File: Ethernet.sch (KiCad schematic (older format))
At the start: 26 parts, among them U5 DM9000B, U6 93LC46, U8 Pulse-J00-0045NL, Y1 25MHz

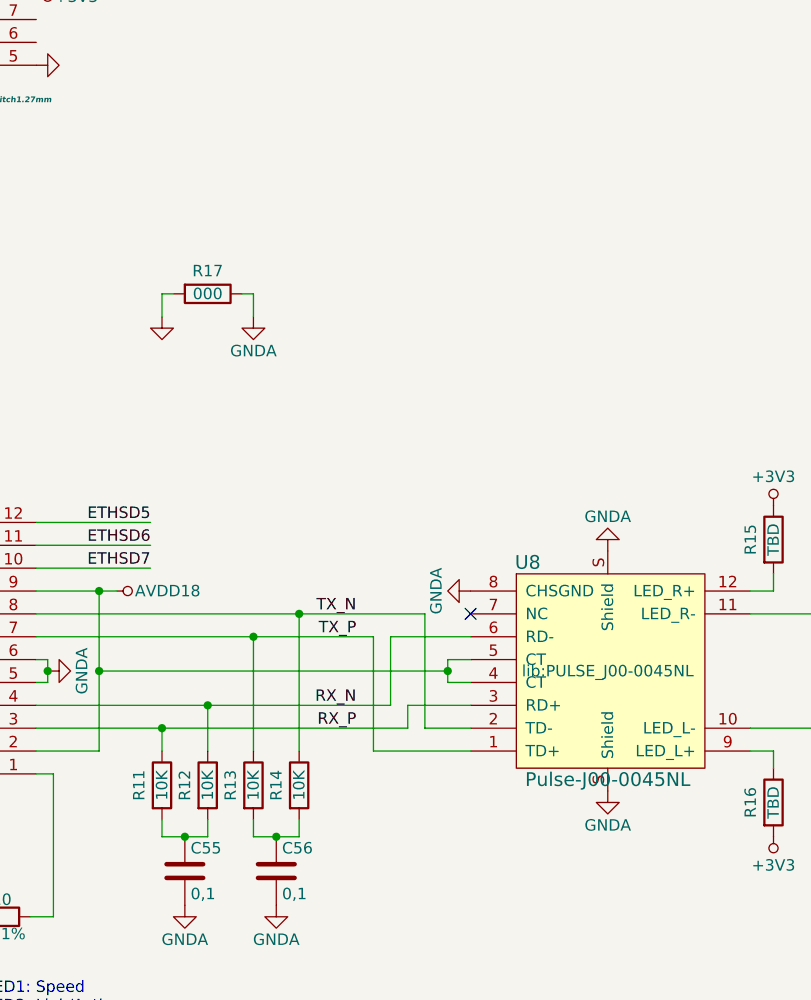
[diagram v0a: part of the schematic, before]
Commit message: Shield copper pour for RJ45
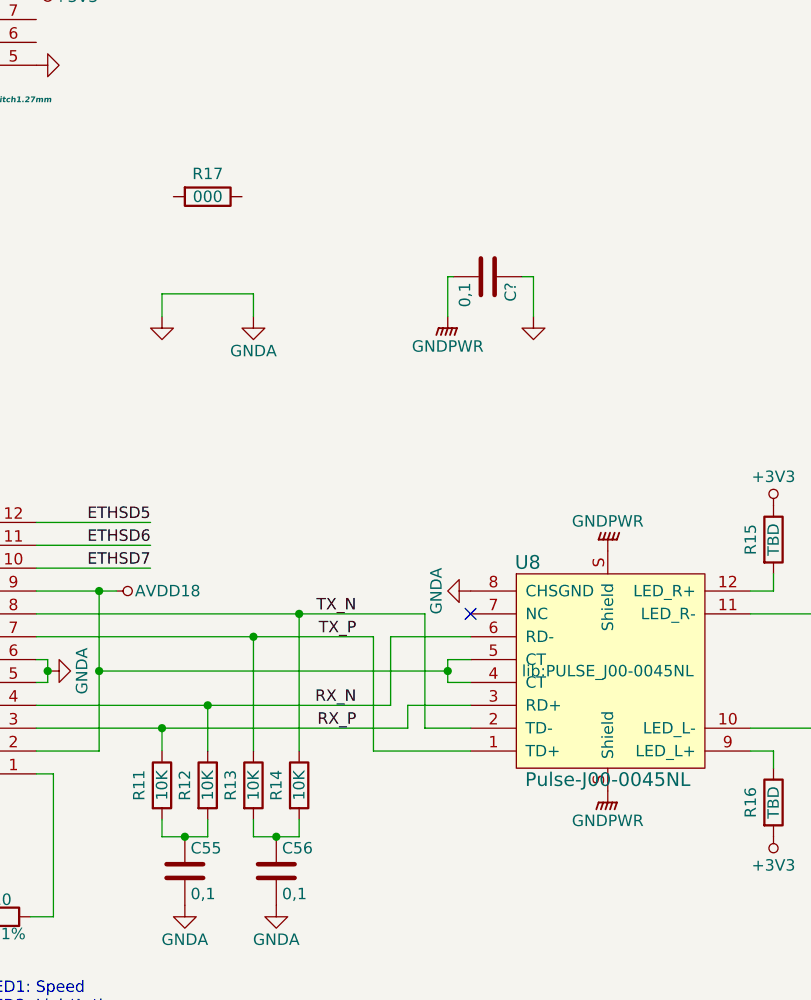
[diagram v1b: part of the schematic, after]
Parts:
- added C?: 0,1, Capacitors_SMD:C_0603, symbol C
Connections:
- net GND: now also C55.2, C56.2, R10.2, U5.47 (RXGND), U5.48 (BGGND), U5.5 (RXGND), U5.6 (TXGND), U8.8 (CHSGND), C?.1; no longer R17.2
- removed net GNDA: C55.2, C56.2, R10.2, R17.1, U5.47 (RXGND), U5.48 (BGGND), U5.5 (RXGND), U5.6 (TXGND), U8.8 (CHSGND), U8.S (Shield)
- new net GNDPWR: C?.2, U8.S (Shield)
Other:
- moved on the sheet: R17
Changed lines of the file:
@@
 $EndComp
 $Comp
-L GND #PWR110
+L GND #PWR0103
 U 1 1 58094372
 P 4850 5575
-F 0 "#PWR110" H 4850 5325 50  0001 C CNN
+F 0 "#PWR0103" H 4850 5325 50  0001 C CNN
 F 1 "GND" H 4850 5425 50  0001 C CNN
 F 2 "" H 4850 5575 50  0000 C CNN
@@
 Connection ~ 4950 6625
 $Comp
-L GNDA #PWR119
+L GNDA #PWR0104
 U 1 1 580972E8
 P 5550 5650
-F 0 "#PWR119" H 5550 5400 50  0001 C CNN
+F 0 "#PWR0104" H 5550 5400 50  0001 C CNN
 F 1 "GNDA" H 5550 5500 50  0000 C CNN
 F 2 "" H 5550 5650 50  0000 C CNN
@@
 Connection ~ 5550 5650
 $Comp
-L GND #PWR115
+L GND #PWR0105
 U 1 1 58097964
 P 5250 5575
-F 0 "#PWR115" H 5250 5325 50  0001 C CNN
+F 0 "#PWR0105" H 5250 5325 50  0001 C CNN
 F 1 "GND" H 5250 5425 50  0001 C CNN
 F 2 "" H 5250 5575 50  0000 C CNN
@@
 $EndComp
 $Comp
-L GND #PWR117
+L GND #PWR0106
 U 1 1 5809797E
 P 5350 3375
-F 0 "#PWR117" H 5350 3125 50  0001 C CNN
+F 0 "#PWR0106" H 5350 3125 50  0001 C CNN
 F 1 "GND" H 5350 3225 50  0001 C CNN
 F 2 "" H 5350 3375 50  0000 C CNN
@@
 $EndComp
 $Comp
-L GND #PWR108
+L GND #PWR0107
 U 1 1 580979A7
 P 3900 4725
-F 0 "#PWR108" H 3900 4475 50  0001 C CNN
+F 0 "#PWR0107" H 3900 4475 50  0001 C CNN
 F 1 "GND" H 3900 4575 50  0001 C CNN
 F 2 "" H 3900 4725 50  0000 C CNN
@@
 $EndComp
 $Comp
-L GND #PWR121
+L GND #PWR0108
 U 1 1 580B3EF3
 P 6100 1925
-F 0 "#PWR121" H 6100 1675 50  0001 C CNN
+F 0 "#PWR0108" H 6100 1675 50  0001 C CNN
 F 1 "GND" H 6100 1775 50  0001 C CNN
 F 2 "" H 6100 1925 50  0000 C CNN
@@
 Connection ~ 2575 6725
 $Comp
-L GND #PWR104
+L GND #PWR0109
 U 1 1 580B6BA7
 P 2300 6725
-F 0 "#PWR104" H 2300 6475 50  0001 C CNN
+F 0 "#PWR0109" H 2300 6475 50  0001 C CNN
 F 1 "GND" H 2300 6575 50  0001 C CNN
 F 2 "" H 2300 6725 50  0000 C CNN
@@
 Connection ~ 2575 6425
 $Comp
-L +3V3 #PWR103
+L +3V3 #PWR0110
 U 1 1 580B8378
 P 2300 6425
-F 0 "#PWR103" H 2400 6475 20  0001 C CNN
+F 0 "#PWR0110" H 2400 6475 20  0001 C CNN
 F 1 "+3V3" H 2300 6550 50  0000 C CNN
 F 2 "" H 2300 6425 60  0000 C CNN
@@
 $EndComp
 $Comp
-L +3V3 #PWR111
+L +3V3 #PWR0111
 U 1 1 580B843E
 P 4950 5700
-F 0 "#PWR111" H 5050 5750 20  0001 C CNN
+F 0 "#PWR0111" H 5050 5750 20  0001 C CNN
 F 1 "+3V3" H 4950 5825 50  0000 C CNN
 F 2 "" H 4950 5700 60  0000 C CNN
@@
 $EndComp
 $Comp
-L +3V3 #PWR107
+L +3V3 #PWR0112
 U 1 1 580B84D9
 P 3775 4425
-F 0 "#PWR107" H 3875 4475 20  0001 C CNN
+F 0 "#PWR0112" H 3875 4475 20  0001 C CNN
 F 1 "+3V3" V 3775 4625 50  0000 C CNN
 F 2 "" H 3775 4425 60  0000 C CNN
@@
 	3775 4425 3900 4425
 $Comp
-L +3V3 #PWR109
+L +3V3 #PWR0113
 U 1 1 580B866E
 P 4550 3225
-F 0 "#PWR109" H 4650 3275 20  0001 C CNN
+F 0 "#PWR0113" H 4650 3275 20  0001 C CNN
 F 1 "+3V3" V 4550 3400 50  0000 C CNN
 F 2 "" H 4550 3225 60  0000 C CNN
@@
 $EndComp
 $Comp
-L GNDA #PWR122
+L GNDA #PWR0114
 U 1 1 580BB313
 P 6150 4575
-F 0 "#PWR122" H 6150 4325 50  0001 C CNN
+F 0 "#PWR0114" H 6150 4325 50  0001 C CNN
 F 1 "GNDA" H 6150 4425 50  0000 C CNN
 F 2 "" H 6150 4575 50  0000 C CNN
@@
 IOW#
 $Comp
-L AVDD18 #PWR123
+L AVDD18 #PWR0115
 U 1 1 580BE743
 P 6450 4225
-F 0 "#PWR123" H 6550 4275 20  0001 C CNN
+F 0 "#PWR0115" H 6550 4275 20  0001 C CNN
 F 1 "AVDD18" V 6450 4450 50  0000 C CNN
 F 2 "" H 6450 4225 60  0000 C CNN
@@
 	2575 7025 2300 7025
 $Comp
-L AVDD18 #PWR105
+L AVDD18 #PWR0116
 U 1 1 580BF8D9
 P 2300 7025
-F 0 "#PWR105" H 2400 7075 20  0001 C CNN
+F 0 "#PWR0116" H 2400 7075 20  0001 C CNN
 F 1 "AVDD18" H 2300 7150 50  0000 C CNN
 F 2 "" H 2300 7025 60  0000 C CNN
@@
 Connection ~ 2300 7025
 $Comp
-L GND #PWR106
+L GND #PWR0117
 U 1 1 580BFAE2
 P 2300 7325
-F 0 "#PWR106" H 2300 7075 50  0001 C CNN
+F 0 "#PWR0117" H 2300 7075 50  0001 C CNN
 F 1 "GND" H 2300 7175 50  0001 C CNN
 F 2 "" H 2300 7325 50  0000 C CNN
@@
 PWRST#
 $Comp
-L GNDA #PWR118
+L GNDA #PWR0118
 U 1 1 580C0A73
 P 5450 5575
-F 0 "#PWR118" H 5450 5325 50  0001 C CNN
+F 0 "#PWR0118" H 5450 5325 50  0001 C CNN
 F 1 "GNDA" H 5450 5425 50  0000 C CNN
 F 2 "" H 5450 5575 50  0000 C CNN
@@
 Connection ~ 4950 1925
 $Comp
-L +3V3 #PWR120
+L +3V3 #PWR0119
 U 1 1 580C1772
 P 6100 1625
-F 0 "#PWR120" H 6200 1675 20  0001 C CNN
+F 0 "#PWR0119" H 6200 1675 20  0001 C CNN
 F 1 "+3V3" V 6100 1800 50  0000 C CNN
 F 2 "" H 6100 1625 60  0000 C CNN
@@
 Connection ~ 6850 4725
 $Comp
-L GNDA #PWR125
+L GNDA #PWR0120
 U 1 1 580C2E4F
 P 6750 5600
-F 0 "#PWR125" H 6750 5350 50  0001 C CNN
+F 0 "#PWR0120" H 6750 5350 50  0001 C CNN
 F 1 "GNDA" H 6750 5450 50  0000 C CNN
 F 2 "" H 6750 5600 50  0000 C CNN
@@
 Connection ~ 7150 5300
 $Comp
-L GNDA #PWR127
+L GNDA #PWR0121
 U 1 1 580C3612
 P 7150 5600
-F 0 "#PWR127" H 7150 5350 50  0001 C CNN
+F 0 "#PWR0121" H 7150 5350 50  0001 C CNN
 F 1 "GNDA" H 7150 5450 50  0000 C CNN
 F 2 "" H 7150 5600 50  0000 C CNN
@@
 	7575 4925 8000 4925
 $Comp
-L GNDA #PWR130
-U 1 1 580C646A
-P 8600 5100
-F 0 "#PWR130" H 8600 4850 50  0001 C CNN
-F 1 "GNDA" H 8600 4950 50  0000 C CNN
-F 2 "" H 8600 5100 50  0000 C CNN
-F 3 "" H 8600 5100 50  0000 C CNN
-	1    8600 5100
-	1    0    0    -1
-$EndComp
-$Comp
-L GNDA #PWR129
-U 1 1 580C64BA
-P 8600 4050
-F 0 "#PWR129" H 8600 3800 50  0001 C CNN
-F 1 "GNDA" H 8600 3900 50  0000 C CNN
-F 2 "" H 8600 4050 50  0000 C CNN
-F 3 "" H 8600 4050 50  0000 C CNN
-	1    8600 4050
-	-1   0    0    1
-$EndComp
-$Comp
-L GNDA #PWR128
+L GNDA #PWR0124
 U 1 1 580C650A
 P 8000 4225
-F 0 "#PWR128" H 8000 3975 50  0001 C CNN
+F 0 "#PWR0124" H 8000 3975 50  0001 C CNN
 F 1 "GNDA" H 8000 4075 50  0000 C CNN
 F 2 "" H 8000 4225 50  0000 C CNN
@@
 	9325 4925 9225 4925
 $Comp
-L +3V3 #PWR131
+L +3V3 #PWR0125
 U 1 1 580CAAEE
 P 9325 3850
-F 0 "#PWR131" H 9425 3900 20  0001 C CNN
+F 0 "#PWR0125" H 9425 3900 20  0001 C CNN
 F 1 "+3V3" H 9325 3975 50  0000 C CNN
 F 2 "" H 9325 3850 60  0000 C CNN
@@
 $EndComp
 $Comp
-L +3V3 #PWR132
+L +3V3 #PWR0126
 U 1 1 580CABDA
 P 9325 5300
-F 0 "#PWR132" H 9425 5350 20  0001 C CNN
+F 0 "#PWR0126" H 9425 5350 20  0001 C CNN
 F 1 "+3V3" H 9325 5425 50  0000 C CNN
 F 2 "" H 9325 5300 60  0000 C CNN
@@
 NoConn ~ 5350 5575
 $Comp
-L GND #PWR124
+L GND #PWR0127
 U 1 1 58165CEB
 P 6650 3025
-F 0 "#PWR124" H 6650 2775 50  0001 C CNN
+F 0 "#PWR0127" H 6650 2775 50  0001 C CNN
 F 1 "GND" H 6650 2875 50  0001 C CNN
 F 2 "" H 6650 3025 50  0000 C CNN
@@
 $EndComp
 $Comp
-L GNDA #PWR126
+L GNDA #PWR0128
 U 1 1 58165E98
 P 7050 3025
-F 0 "#PWR126" H 7050 2775 50  0001 C CNN
+F 0 "#PWR0128" H 7050 2775 50  0001 C CNN
 F 1 "GNDA" H 7050 2875 50  0000 C CNN
 F 2 "" H 7050 3025 50  0000 C CNN
@@
 L R R17
 U 1 1 58165F7B
-P 6850 2925
-F 0 "R17" V 6750 2925 50  0000 C CNN
-F 1 "000" V 6850 2925 50  0000 C CNN
-F 2 "Resistors_SMD:R_0603" V 6780 2925 50  0001 C CNN
-F 3 "" H 6850 2925 50  0000 C CNN
-	1    6850 2925
+P 6850 2500
+F 0 "R17" V 6750 2500 50  0000 C CNN
+F 1 "000" V 6850 2500 50  0000 C CNN
+F 2 "Resistors_SMD:R_0603" V 6780 2500 50  0001 C CNN
+F 3 "" H 6850 2500 50  0000 C CNN
+	1    6850 2500
 	0    1    1    0
 $EndComp
 Wire Wire Line
-	6700 2925 6650 2925
+	6650 2925 7050 2925
 Wire Wire Line
 	6650 2925 6650 3025
 Wire Wire Line
-	7050 3025 7050 2925
-Wire Wire Line
-	7050 2925 7000 2925
+	7050 2925 7050 3025
 Wire Bus Line
 	1900 1100 1900 2800
@@
 	1900 2800 2000 2900
 $Comp
-L GND #PWR116
+L GND #PWR0129
 U 1 1 5893DA80
 P 5250 7125
-F 0 "#PWR116" H 5250 6875 50  0001 C CNN
+F 0 "#PWR0129" H 5250 6875 50  0001 C CNN
 F 1 "GND" H 5250 6975 50  0001 C CNN
 F 2 "" H 5250 7125 50  0000 C CNN
@@
 $EndComp
 $Comp
-L GND #PWR112
+L GND #PWR0130
 U 1 1 5893DB6B
 P 4950 7125
-F 0 "#PWR112" H 4950 6875 50  0001 C CNN
+F 0 "#PWR0130" H 4950 6875 50  0001 C CNN
 F 1 "GND" H 4950 6975 50  0001 C CNN
 F 2 "" H 4950 7125 50  0000 C CNN
@@
 $EndComp
 $Comp
-L GND #PWR114
+L GND #PWR0131
 U 1 1 5893E3B5
 P 5100 6825
-F 0 "#PWR114" H 5100 6575 50  0001 C CNN
+F 0 "#PWR0131" H 5100 6575 50  0001 C CNN
 F 1 "GND" H 5100 6675 50  0001 C CNN
 F 2 "" H 5100 6825 50  0000 C CNN
@@
 $EndComp
 $Comp
-L GND #PWR113
+L GND #PWR0132
 U 1 1 5893E40E
 P 5100 6425
-F 0 "#PWR113" H 5100 6175 50  0001 C CNN
+F 0 "#PWR0132" H 5100 6175 50  0001 C CNN
 F 1 "GND" H 5100 6275 50  0001 C CNN
 F 2 "" H 5100 6425 50  0000 C CNN
@@
 	-1   0    0    1
 $EndComp
+$Comp
+L GNDPWR #PWR?
+U 1 1 589CDFD0
+P 8600 4050
+F 0 "#PWR?" H 8600 3850 50  0001 C CNN
+F 1 "GNDPWR" H 8600 3920 50  0000 C CNN
+F 2 "" H 8600 4000 50  0000 C CNN
+F 3 "" H 8600 4000 50  0000 C CNN
+	1    8600 4050
+	-1   0    0    1
+$EndComp
+$Comp
+L GNDPWR #PWR?
+U 1 1 589CE07E
+P 8600 5100
+F 0 "#PWR?" H 8600 4900 50  0001 C CNN
+F 1 "GNDPWR" H 8600 4970 50  0000 C CNN
+F 2 "" H 8600 5050 50  0000 C CNN
+F 3 "" H 8600 5050 50  0000 C CNN
+	1    8600 5100
+	1    0    0    -1
+$EndComp
+$Comp
+L GNDPWR #PWR?
+U 1 1 589CE0D7
+P 7900 3025
+F 0 "#PWR?" H 7900 2825 50  0001 C CNN
+F 1 "GNDPWR" H 7900 2895 50  0000 C CNN
+F 2 "" H 7900 2975 50  0000 C CNN
+F 3 "" H 7900 2975 50  0000 C CNN
+	1    7900 3025
+	1    0    0    -1
+$EndComp
+$Comp
+L C C?
+U 1 1 589CE24E
+P 8075 2850
+F 0 "C?" H 8100 2950 50  0000 L CNN
+F 1 "0,1" H 8100 2750 50  0000 L CNN
+F 2 "Capacitors_SMD:C_0603" H 8113 2700 50  0001 C CNN
+F 3 "" H 8075 2850 50  0000 C CNN
+	1    8075 2850
+	0    1    1    0
+$EndComp
+$Comp
+L GND #PWR?
+U 1 1 589CE36B
+P 8275 3025
+F 0 "#PWR?" H 8275 2775 50  0001 C CNN
+F 1 "GND" H 8275 2875 50  0001 C CNN
+F 2 "" H 8275 3025 50  0000 C CNN
+F 3 "" H 8275 3025 50  0000 C CNN
+	1    8275 3025
+	1    0    0    -1
+$EndComp
+Wire Wire Line
+	8225 2850 8275 2850
+Wire Wire Line
+	8275 2850 8275 3025
+Wire Wire Line
+	7925 2850 7900 2850
+Wire Wire Line
+	7900 2850 7900 3025
 $EndSCHEMATC

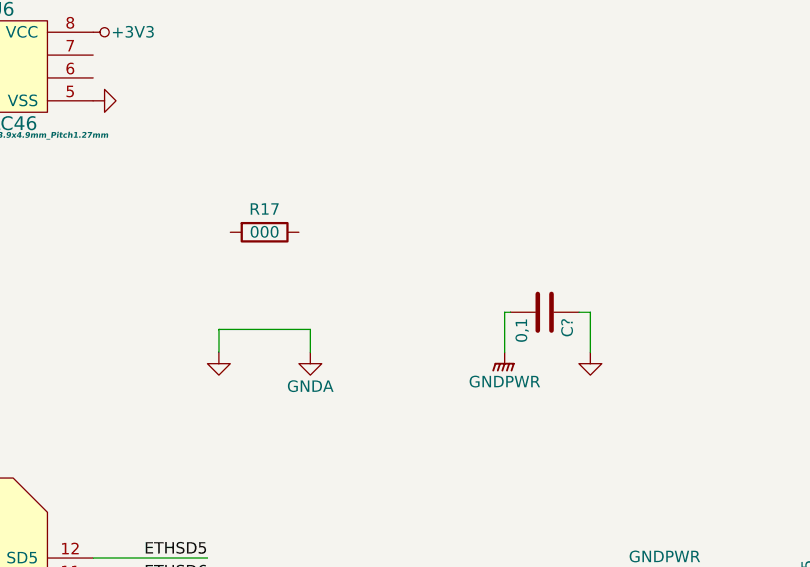
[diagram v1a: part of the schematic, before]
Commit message: TX/RX pairs routed
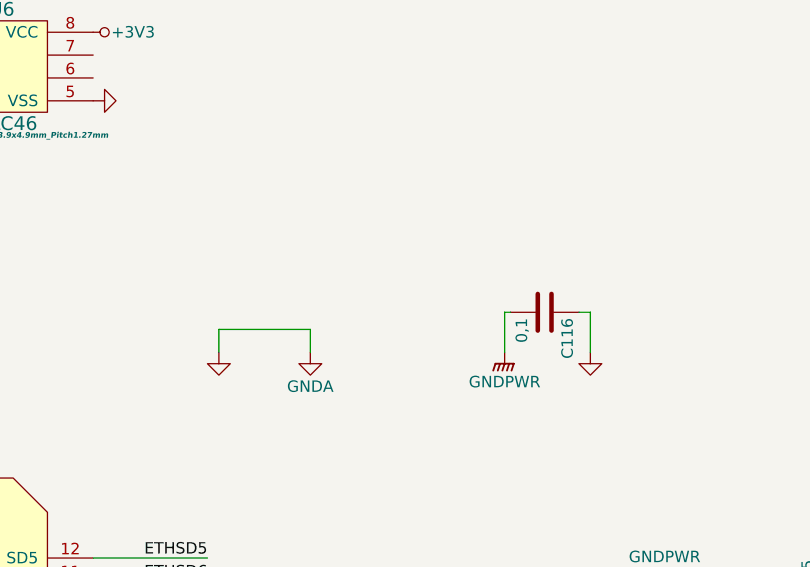
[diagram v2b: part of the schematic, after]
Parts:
- removed R17: 000, Resistors_SMD:R_0603, symbol R
- C50: footprint (none) -> Capacitors_Tantalum_SMD:CP_Tantalum_Case-B_EIA-3528-21_Reflow
- gave numbers to parts that had none: 1
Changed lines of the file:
@@
 F 0 "C50" H 2600 7275 50  0000 L CNN
 F 1 "220x16" H 2600 7075 50  0000 L CNN
-F 2 "" H 2575 7175 50  0001 C CNN
+F 2 "Capacitors_Tantalum_SMD:CP_Tantalum_Case-B_EIA-3528-21_Reflow" H 2575 7175 50  0001 C CNN
 F 3 "" H 2575 7175 50  0000 C CNN
 	1    2575 7175
@@
 	7575 4925 8000 4925
 $Comp
-L GNDA #PWR0124
+L GNDA #PWR0122
 U 1 1 580C650A
 P 8000 4225
-F 0 "#PWR0124" H 8000 3975 50  0001 C CNN
+F 0 "#PWR0122" H 8000 3975 50  0001 C CNN
 F 1 "GNDA" H 8000 4075 50  0000 C CNN
 F 2 "" H 8000 4225 50  0000 C CNN
@@
 	9325 4925 9225 4925
 $Comp
-L +3V3 #PWR0125
+L +3V3 #PWR0123
 U 1 1 580CAAEE
 P 9325 3850
-F 0 "#PWR0125" H 9425 3900 20  0001 C CNN
+F 0 "#PWR0123" H 9425 3900 20  0001 C CNN
 F 1 "+3V3" H 9325 3975 50  0000 C CNN
 F 2 "" H 9325 3850 60  0000 C CNN
@@
 $EndComp
 $Comp
-L +3V3 #PWR0126
+L +3V3 #PWR0124
 U 1 1 580CABDA
 P 9325 5300
-F 0 "#PWR0126" H 9425 5350 20  0001 C CNN
+F 0 "#PWR0124" H 9425 5350 20  0001 C CNN
 F 1 "+3V3" H 9325 5425 50  0000 C CNN
 F 2 "" H 9325 5300 60  0000 C CNN
@@
 NoConn ~ 5350 5575
 $Comp
-L GND #PWR0127
+L GND #PWR0125
 U 1 1 58165CEB
 P 6650 3025
-F 0 "#PWR0127" H 6650 2775 50  0001 C CNN
+F 0 "#PWR0125" H 6650 2775 50  0001 C CNN
 F 1 "GND" H 6650 2875 50  0001 C CNN
 F 2 "" H 6650 3025 50  0000 C CNN
@@
 $EndComp
 $Comp
-L GNDA #PWR0128
+L GNDA #PWR0126
 U 1 1 58165E98
 P 7050 3025
-F 0 "#PWR0128" H 7050 2775 50  0001 C CNN
+F 0 "#PWR0126" H 7050 2775 50  0001 C CNN
 F 1 "GNDA" H 7050 2875 50  0000 C CNN
 F 2 "" H 7050 3025 50  0000 C CNN
@@
 	1    7050 3025
 	1    0    0    -1
-$EndComp
-$Comp
-L R R17
-U 1 1 58165F7B
-P 6850 2500
-F 0 "R17" V 6750 2500 50  0000 C CNN
-F 1 "000" V 6850 2500 50  0000 C CNN
-F 2 "Resistors_SMD:R_0603" V 6780 2500 50  0001 C CNN
-F 3 "" H 6850 2500 50  0000 C CNN
-	1    6850 2500
-	0    1    1    0
 $EndComp
 Wire Wire Line
@@
 	1900 2800 2000 2900
 $Comp
-L GND #PWR0129
+L GND #PWR0127
 U 1 1 5893DA80
 P 5250 7125
-F 0 "#PWR0129" H 5250 6875 50  0001 C CNN
+F 0 "#PWR0127" H 5250 6875 50  0001 C CNN
 F 1 "GND" H 5250 6975 50  0001 C CNN
 F 2 "" H 5250 7125 50  0000 C CNN
@@
 $EndComp
 $Comp
-L GND #PWR0130
+L GND #PWR0128
 U 1 1 5893DB6B
 P 4950 7125
-F 0 "#PWR0130" H 4950 6875 50  0001 C CNN
+F 0 "#PWR0128" H 4950 6875 50  0001 C CNN
 F 1 "GND" H 4950 6975 50  0001 C CNN
 F 2 "" H 4950 7125 50  0000 C CNN
@@
 $EndComp
 $Comp
-L GND #PWR0131
+L GND #PWR0129
 U 1 1 5893E3B5
 P 5100 6825
-F 0 "#PWR0131" H 5100 6575 50  0001 C CNN
+F 0 "#PWR0129" H 5100 6575 50  0001 C CNN
 F 1 "GND" H 5100 6675 50  0001 C CNN
 F 2 "" H 5100 6825 50  0000 C CNN
@@
 $EndComp
 $Comp
-L GND #PWR0132
+L GND #PWR0130
 U 1 1 5893E40E
 P 5100 6425
-F 0 "#PWR0132" H 5100 6175 50  0001 C CNN
+F 0 "#PWR0130" H 5100 6175 50  0001 C CNN
 F 1 "GND" H 5100 6275 50  0001 C CNN
 F 2 "" H 5100 6425 50  0000 C CNN
@@
 $EndComp
 $Comp
-L GNDPWR #PWR?
+L GNDPWR #PWR0131
 U 1 1 589CDFD0
 P 8600 4050
-F 0 "#PWR?" H 8600 3850 50  0001 C CNN
+F 0 "#PWR0131" H 8600 3850 50  0001 C CNN
 F 1 "GNDPWR" H 8600 3920 50  0000 C CNN
 F 2 "" H 8600 4000 50  0000 C CNN
@@
 $EndComp
 $Comp
-L GNDPWR #PWR?
+L GNDPWR #PWR0132
 U 1 1 589CE07E
 P 8600 5100
-F 0 "#PWR?" H 8600 4900 50  0001 C CNN
+F 0 "#PWR0132" H 8600 4900 50  0001 C CNN
 F 1 "GNDPWR" H 8600 4970 50  0000 C CNN
 F 2 "" H 8600 5050 50  0000 C CNN
@@
 $EndComp
 $Comp
-L GNDPWR #PWR?
+L GNDPWR #PWR0133
 U 1 1 589CE0D7
 P 7900 3025
-F 0 "#PWR?" H 7900 2825 50  0001 C CNN
+F 0 "#PWR0133" H 7900 2825 50  0001 C CNN
 F 1 "GNDPWR" H 7900 2895 50  0000 C CNN
 F 2 "" H 7900 2975 50  0000 C CNN
@@
 $EndComp
 $Comp
-L C C?
+L C C116
 U 1 1 589CE24E
 P 8075 2850
-F 0 "C?" H 8100 2950 50  0000 L CNN
+F 0 "C116" H 8100 2950 50  0000 L CNN
 F 1 "0,1" H 8100 2750 50  0000 L CNN
 F 2 "Capacitors_SMD:C_0603" H 8113 2700 50  0001 C CNN
@@
 $EndComp
 $Comp
-L GND #PWR?
+L GND #PWR0134
 U 1 1 589CE36B
 P 8275 3025
-F 0 "#PWR?" H 8275 2775 50  0001 C CNN
+F 0 "#PWR0134" H 8275 2775 50  0001 C CNN
 F 1 "GND" H 8275 2875 50  0001 C CNN
 F 2 "" H 8275 3025 50  0000 C CNN
